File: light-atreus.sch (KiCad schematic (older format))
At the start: 1 part

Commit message: Completely redesign everything
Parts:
- removed U?: TUSB320, symbol TUSB320
- added J? (x2): USB_OTG, symbol USB_OTG
- added J? (x2): CONN_01X02, symbol CONN_01X02
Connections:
- net labels added: GND
- wire segments 0 -> 14
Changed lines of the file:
@@
 LIBS:valves
 LIBS:project
-EELAYER 25 0
+LIBS:light-atreus-cache
+EELAYER 26 0
 EELAYER END
 $Descr A4 11693 8268
@@
 $EndDescr
 $Comp
-L TUSB320 U?
-U 1 1 597ED03E
-P 5950 3850
-F 0 "U?" H 6350 4400 60  0000 C CNN
-F 1 "TUSB320" H 5450 4300 60  0000 C CNN
-F 2 "" H 5550 3900 60  0001 C CNN
-F 3 "" H 5550 3900 60  0001 C CNN
-	1    5950 3850
+L USB_OTG J?
+U 1 1 59C6CA5B
+P 3500 3850
+F 0 "J?" H 3555 4317 50  0000 C CNN
+F 1 "USB_OTG" H 3555 4226 50  0000 C CNN
+F 2 "" H 3650 3800 50  0001 C CNN
+F 3 "" H 3650 3800 50  0001 C CNN
+	1    3500 3850
 	1    0    0    -1
 $EndComp
+$Comp
+L USB_OTG J?
+U 1 1 59C6CAF0
+P 6000 3850
+F 0 "J?" H 6056 4317 50  0000 C CNN
+F 1 "USB_OTG" H 6056 4226 50  0000 C CNN
+F 2 "" H 6150 3800 50  0001 C CNN
+F 3 "" H 6150 3800 50  0001 C CNN
+	1    6000 3850
+	-1   0    0    -1
+$EndComp
+Wire Wire Line
+	3800 3650 5700 3650
+Wire Wire Line
+	3800 3850 5700 3850
+Wire Wire Line
+	3800 3950 5700 3950
+Wire Wire Line
+	3800 4050 5700 4050
+Wire Wire Line
+	3500 4250 3500 4350
+Wire Wire Line
+	3500 4350 6000 4350
+Wire Wire Line
+	6000 4350 6000 4250
+Wire Wire Line
+	3400 4250 3400 4450
+Wire Wire Line
+	3400 4450 6100 4450
+Wire Wire Line
+	6100 4450 6100 4250
+Wire Wire Line
+	4750 3350 4750 4550
+Connection ~ 4750 4450
+Connection ~ 4750 4350
+$Comp
+L GND #PWR?
+U 1 1 59C6CDCA
+P 4750 4550
+F 0 "#PWR?" H 4750 4300 50  0001 C CNN
+F 1 "GND" H 4755 4377 50  0000 C CNN
+F 2 "" H 4750 4550 50  0001 C CNN
+F 3 "" H 4750 4550 50  0001 C CNN
+	1    4750 4550
+	1    0    0    -1
+$EndComp
+$Comp
+L CONN_01X02 J?
+U 1 1 59C6CECB
+P 5050 3300
+F 0 "J?" H 5128 3341 50  0000 L CNN
+F 1 "CONN_01X02" H 5128 3250 50  0000 L CNN
+F 2 "" H 5050 3300 50  0001 C CNN
+F 3 "" H 5050 3300 50  0001 C CNN
+	1    5050 3300
+	1    0    0    -1
+$EndComp
+Wire Wire Line
+	4400 3250 4850 3250
+Wire Wire Line
+	4600 3250 4600 3650
+Connection ~ 4600 3650
+Wire Wire Line
+	4400 3350 4850 3350
+$Comp
+L CONN_01X02 J?
+U 1 1 59C6D03C
+P 4200 3300
+F 0 "J?" H 4278 3341 50  0000 L CNN
+F 1 "CONN_01X02" H 4278 3250 50  0000 L CNN
+F 2 "" H 4200 3300 50  0001 C CNN
+F 3 "" H 4200 3300 50  0001 C CNN
+	1    4200 3300
+	-1   0    0    -1
+$EndComp
+Connection ~ 4750 3350
+Connection ~ 4600 3250
 $EndSCHEMATC

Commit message: Use 4-pin connectors for doing fish-hook
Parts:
- removed J? (x2): CONN_01X02, symbol CONN_01X02
- added J? (x2): CONN_01X04, symbol CONN_01X04
- J? (x2): footprint (none) -> Connectors:USB_Micro-B
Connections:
- net labels removed: GND
- no-connect marks 0 -> 4
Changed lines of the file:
@@
 F 0 "J?" H 3555 4317 50  0000 C CNN
 F 1 "USB_OTG" H 3555 4226 50  0000 C CNN
-F 2 "" H 3650 3800 50  0001 C CNN
+F 2 "Connectors:USB_Micro-B" H 3650 3800 50  0001 C CNN
 F 3 "" H 3650 3800 50  0001 C CNN
 	1    3500 3850
@@
 F 0 "J?" H 6056 4317 50  0000 C CNN
 F 1 "USB_OTG" H 6056 4226 50  0000 C CNN
-F 2 "" H 6150 3800 50  0001 C CNN
+F 2 "Connectors:USB_Micro-B" H 6150 3800 50  0001 C CNN
 F 3 "" H 6150 3800 50  0001 C CNN
 	1    6000 3850
@@
 	3800 3950 5700 3950
 Wire Wire Line
-	3800 4050 5700 4050
-Wire Wire Line
 	3500 4250 3500 4350
 Wire Wire Line
@@
 	3400 4250 3400 4450
 Wire Wire Line
-	3400 4450 6100 4450
-Wire Wire Line
 	6100 4450 6100 4250
-Wire Wire Line
-	4750 3350 4750 4550
-Connection ~ 4750 4450
-Connection ~ 4750 4350
-$Comp
-L GND #PWR?
-U 1 1 59C6CDCA
-P 4750 4550
-F 0 "#PWR?" H 4750 4300 50  0001 C CNN
-F 1 "GND" H 4755 4377 50  0000 C CNN
-F 2 "" H 4750 4550 50  0001 C CNN
-F 3 "" H 4750 4550 50  0001 C CNN
-	1    4750 4550
-	1    0    0    -1
-$EndComp
-$Comp
-L CONN_01X02 J?
-U 1 1 59C6CECB
-P 5050 3300
-F 0 "J?" H 5128 3341 50  0000 L CNN
-F 1 "CONN_01X02" H 5128 3250 50  0000 L CNN
-F 2 "" H 5050 3300 50  0001 C CNN
-F 3 "" H 5050 3300 50  0001 C CNN
-	1    5050 3300
-	1    0    0    -1
-$EndComp
 Wire Wire Line
 	4400 3250 4850 3250
@@
 Wire Wire Line
 	4400 3350 4850 3350
+Connection ~ 4750 3350
+Connection ~ 4600 3250
 $Comp
-L CONN_01X02 J?
-U 1 1 59C6D03C
+L CONN_01X04 J?
+U 1 1 59C6D991
+P 5050 3300
+F 0 "J?" H 5128 3341 50  0000 L CNN
+F 1 "CONN_01X04" H 5128 3250 50  0000 L CNN
+F 2 "" H 5050 3300 50  0001 C CNN
+F 3 "" H 5050 3300 50  0001 C CNN
+	1    5050 3300
+	1    0    0    -1
+$EndComp
+$Comp
+L CONN_01X04 J?
+U 1 1 59C6D9ED
 P 4200 3300
 F 0 "J?" H 4278 3341 50  0000 L CNN
-F 1 "CONN_01X02" H 4278 3250 50  0000 L CNN
+F 1 "CONN_01X04" H 4278 3250 50  0000 L CNN
 F 2 "" H 4200 3300 50  0001 C CNN
 F 3 "" H 4200 3300 50  0001 C CNN
@@
 	-1   0    0    -1
 $EndComp
-Connection ~ 4750 3350
-Connection ~ 4600 3250
+NoConn ~ 4850 3450
+NoConn ~ 4850 3150
+NoConn ~ 4400 3150
+NoConn ~ 4400 3450
+Wire Wire Line
+	3400 4450 6100 4450
+Wire Wire Line
+	4750 3350 4750 4350
+Connection ~ 4750 4350
+Wire Wire Line
+	3800 4050 5700 4050
 $EndSCHEMATC

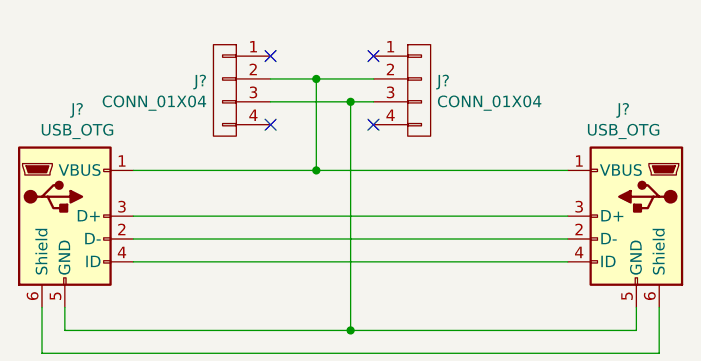
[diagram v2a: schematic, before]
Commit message: Use 2x2 instead of 1x4 headers
That way the arrangement will put the holder hole nearer to the outer
edge of the board.
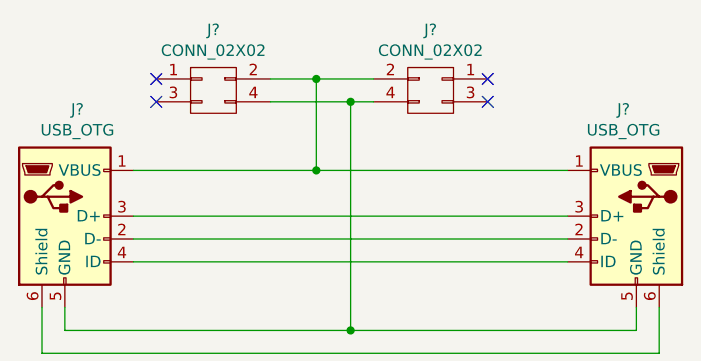
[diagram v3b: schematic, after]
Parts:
- removed J? (x2): CONN_01X04, symbol CONN_01X04
- added J? (x2): CONN_02X02, symbol CONN_02X02
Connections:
- net at J?.1 (VBUS), J?.1 (VBUS): now also J?.2 (P2), J?.2 (P2)
- net at J?.5 (GND), J?.5 (GND): now also J?.4 (P4), J?.4 (P4)
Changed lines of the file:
@@
 Connection ~ 4750 3350
 Connection ~ 4600 3250
-$Comp
-L CONN_01X04 J?
-U 1 1 59C6D991
-P 5050 3300
-F 0 "J?" H 5128 3341 50  0000 L CNN
-F 1 "CONN_01X04" H 5128 3250 50  0000 L CNN
-F 2 "" H 5050 3300 50  0001 C CNN
-F 3 "" H 5050 3300 50  0001 C CNN
-	1    5050 3300
-	1    0    0    -1
-$EndComp
-$Comp
-L CONN_01X04 J?
-U 1 1 59C6D9ED
-P 4200 3300
-F 0 "J?" H 4278 3341 50  0000 L CNN
-F 1 "CONN_01X04" H 4278 3250 50  0000 L CNN
-F 2 "" H 4200 3300 50  0001 C CNN
-F 3 "" H 4200 3300 50  0001 C CNN
-	1    4200 3300
-	-1   0    0    -1
-$EndComp
-NoConn ~ 4850 3450
-NoConn ~ 4850 3150
-NoConn ~ 4400 3150
-NoConn ~ 4400 3450
 Wire Wire Line
 	3400 4450 6100 4450
@@
 Wire Wire Line
 	3800 4050 5700 4050
+$Comp
+L CONN_02X02 J?
+U 1 1 59CAC2E2
+P 4150 3300
+F 0 "J?" H 4150 3565 50  0000 C CNN
+F 1 "CONN_02X02" H 4150 3474 50  0000 C CNN
+F 2 "" H 4150 2100 50  0001 C CNN
+F 3 "" H 4150 2100 50  0001 C CNN
+	1    4150 3300
+	1    0    0    -1
+$EndComp
+$Comp
+L CONN_02X02 J?
+U 1 1 59CAC352
+P 5100 3300
+F 0 "J?" H 5100 3565 50  0000 C CNN
+F 1 "CONN_02X02" H 5100 3474 50  0000 C CNN
+F 2 "" H 5100 2100 50  0001 C CNN
+F 3 "" H 5100 2100 50  0001 C CNN
+	1    5100 3300
+	-1   0    0    -1
+$EndComp
+NoConn ~ 5350 3250
+NoConn ~ 5350 3350
+NoConn ~ 3900 3350
+NoConn ~ 3900 3250
 $EndSCHEMATC

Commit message: Annotate and generate netlist
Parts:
- gave numbers to parts that had none: 4
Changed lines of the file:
@@
 $EndDescr
 $Comp
-L USB_OTG J?
+L USB_OTG J1
 U 1 1 59C6CA5B
 P 3500 3850
-F 0 "J?" H 3555 4317 50  0000 C CNN
+F 0 "J1" H 3555 4317 50  0000 C CNN
 F 1 "USB_OTG" H 3555 4226 50  0000 C CNN
 F 2 "Connectors:USB_Micro-B" H 3650 3800 50  0001 C CNN
@@
 $EndComp
 $Comp
-L USB_OTG J?
+L USB_OTG J4
 U 1 1 59C6CAF0
 P 6000 3850
-F 0 "J?" H 6056 4317 50  0000 C CNN
+F 0 "J4" H 6056 4317 50  0000 C CNN
 F 1 "USB_OTG" H 6056 4226 50  0000 C CNN
 F 2 "Connectors:USB_Micro-B" H 6150 3800 50  0001 C CNN
@@
 	3800 4050 5700 4050
 $Comp
-L CONN_02X02 J?
+L CONN_02X02 J2
 U 1 1 59CAC2E2
 P 4150 3300
-F 0 "J?" H 4150 3565 50  0000 C CNN
+F 0 "J2" H 4150 3565 50  0000 C CNN
 F 1 "CONN_02X02" H 4150 3474 50  0000 C CNN
 F 2 "" H 4150 2100 50  0001 C CNN
@@
 $EndComp
 $Comp
-L CONN_02X02 J?
+L CONN_02X02 J3
 U 1 1 59CAC352
 P 5100 3300
-F 0 "J?" H 5100 3565 50  0000 C CNN
+F 0 "J3" H 5100 3565 50  0000 C CNN
 F 1 "CONN_02X02" H 5100 3474 50  0000 C CNN
 F 2 "" H 5100 2100 50  0001 C CNN

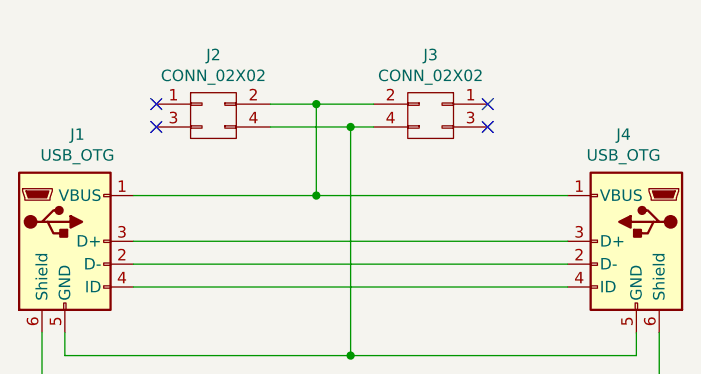
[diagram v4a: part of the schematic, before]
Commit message: Use banana jack connector pads
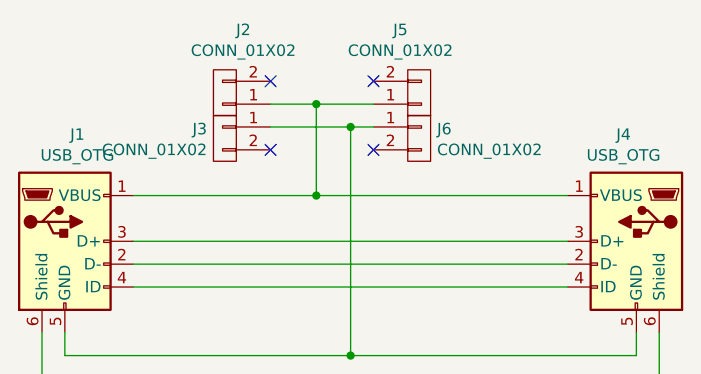
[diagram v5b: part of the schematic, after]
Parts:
- removed J2, J3: CONN_02X02, symbol CONN_02X02
- added J2, J3, J5, J6: CONN_01X02, Connectors:Banana_Jack_2Pin, symbol CONN_01X02
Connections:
- net at J1.1 (VBUS), J4.1 (VBUS): now also J2.1 (P1), J5.1 (P1)
- net at J1.5 (GND), J4.5 (GND): now also J3.1 (P1), J6.1 (P1)
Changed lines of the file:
@@
 	3800 4050 5700 4050
 $Comp
-L CONN_02X02 J2
-U 1 1 59CAC2E2
-P 4150 3300
-F 0 "J2" H 4150 3565 50  0000 C CNN
-F 1 "CONN_02X02" H 4150 3474 50  0000 C CNN
-F 2 "" H 4150 2100 50  0001 C CNN
-F 3 "" H 4150 2100 50  0001 C CNN
-	1    4150 3300
+L CONN_01X02 J2
+U 1 1 59CAC5DC
+P 4200 3200
+F 0 "J2" H 4119 2925 50  0000 C CNN
+F 1 "CONN_01X02" H 4119 3016 50  0000 C CNN
+F 2 "Connectors:Banana_Jack_2Pin" H 4200 3200 50  0001 C CNN
+F 3 "" H 4200 3200 50  0001 C CNN
+	1    4200 3200
+	-1   0    0    1
+$EndComp
+$Comp
+L CONN_01X02 J3
+U 1 1 59CAC664
+P 4200 3400
+F 0 "J3" H 4278 3441 50  0000 L CNN
+F 1 "CONN_01X02" H 4278 3350 50  0000 L CNN
+F 2 "Connectors:Banana_Jack_2Pin" H 4200 3400 50  0001 C CNN
+F 3 "" H 4200 3400 50  0001 C CNN
+	1    4200 3400
+	-1   0    0    -1
+$EndComp
+$Comp
+L CONN_01X02 J5
+U 1 1 59CAC690
+P 5050 3200
+F 0 "J5" H 4968 2925 50  0000 C CNN
+F 1 "CONN_01X02" H 4968 3016 50  0000 C CNN
+F 2 "Connectors:Banana_Jack_2Pin" H 5050 3200 50  0001 C CNN
+F 3 "" H 5050 3200 50  0001 C CNN
+	1    5050 3200
+	1    0    0    1
+$EndComp
+$Comp
+L CONN_01X02 J6
+U 1 1 59CAC6F5
+P 5050 3400
+F 0 "J6" H 5128 3441 50  0000 L CNN
+F 1 "CONN_01X02" H 5128 3350 50  0000 L CNN
+F 2 "Connectors:Banana_Jack_2Pin" H 5050 3400 50  0001 C CNN
+F 3 "" H 5050 3400 50  0001 C CNN
+	1    5050 3400
 	1    0    0    -1
 $EndComp
-$Comp
-L CONN_02X02 J3
-U 1 1 59CAC352
-P 5100 3300
-F 0 "J3" H 5100 3565 50  0000 C CNN
-F 1 "CONN_02X02" H 5100 3474 50  0000 C CNN
-F 2 "" H 5100 2100 50  0001 C CNN
-F 3 "" H 5100 2100 50  0001 C CNN
-	1    5100 3300
-	-1   0    0    -1
-$EndComp
-NoConn ~ 5350 3250
-NoConn ~ 5350 3350
-NoConn ~ 3900 3350
-NoConn ~ 3900 3250
+NoConn ~ 4850 3450
+NoConn ~ 4850 3150
+NoConn ~ 4400 3150
+NoConn ~ 4400 3450
 $EndSCHEMATC

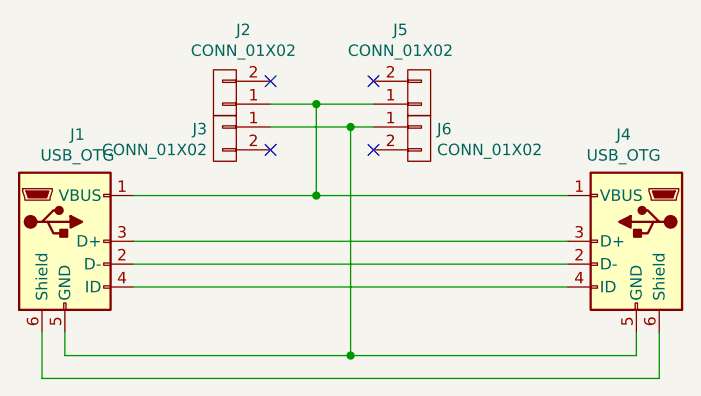
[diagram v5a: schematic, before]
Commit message: Name nets on broken out pins
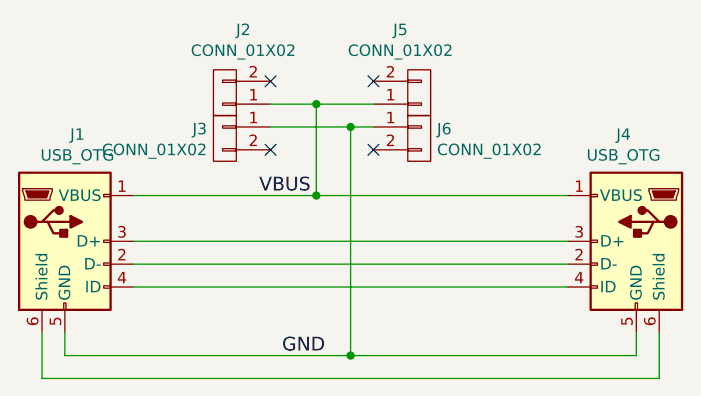
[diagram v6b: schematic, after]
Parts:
- J2, J3, J5, J6: footprint Connectors:Banana_Jack_2Pin -> custom_footprints:SolderWirePad_1x2-8mm
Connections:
- net VBUS: now reaches J1.1 (VBUS), J2.1 (P1), J4.1 (VBUS), J5.1 (P1)
- net GND: now reaches J1.5 (GND), J3.1 (P1), J4.5 (GND), J6.1 (P1)
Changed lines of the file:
@@
 F 0 "J2" H 4119 2925 50  0000 C CNN
 F 1 "CONN_01X02" H 4119 3016 50  0000 C CNN
-F 2 "Connectors:Banana_Jack_2Pin" H 4200 3200 50  0001 C CNN
+F 2 "custom_footprints:SolderWirePad_1x2-8mm" H 4200 3200 50  0001 C CNN
 F 3 "" H 4200 3200 50  0001 C CNN
 	1    4200 3200
@@
 F 0 "J3" H 4278 3441 50  0000 L CNN
 F 1 "CONN_01X02" H 4278 3350 50  0000 L CNN
-F 2 "Connectors:Banana_Jack_2Pin" H 4200 3400 50  0001 C CNN
+F 2 "custom_footprints:SolderWirePad_1x2-8mm" H 4200 3400 50  0001 C CNN
 F 3 "" H 4200 3400 50  0001 C CNN
 	1    4200 3400
@@
 F 0 "J5" H 4968 2925 50  0000 C CNN
 F 1 "CONN_01X02" H 4968 3016 50  0000 C CNN
-F 2 "Connectors:Banana_Jack_2Pin" H 5050 3200 50  0001 C CNN
+F 2 "custom_footprints:SolderWirePad_1x2-8mm" H 5050 3200 50  0001 C CNN
 F 3 "" H 5050 3200 50  0001 C CNN
 	1    5050 3200
@@
 F 0 "J6" H 5128 3441 50  0000 L CNN
 F 1 "CONN_01X02" H 5128 3350 50  0000 L CNN
-F 2 "Connectors:Banana_Jack_2Pin" H 5050 3400 50  0001 C CNN
+F 2 "custom_footprints:SolderWirePad_1x2-8mm" H 5050 3400 50  0001 C CNN
 F 3 "" H 5050 3400 50  0001 C CNN
 	1    5050 3400
@@
 NoConn ~ 4400 3150
 NoConn ~ 4400 3450
+Text Label 4450 4350 0    60   ~ 0
+GND
+Text Label 4350 3650 0    60   ~ 0
+VBUS
 $EndSCHEMATC

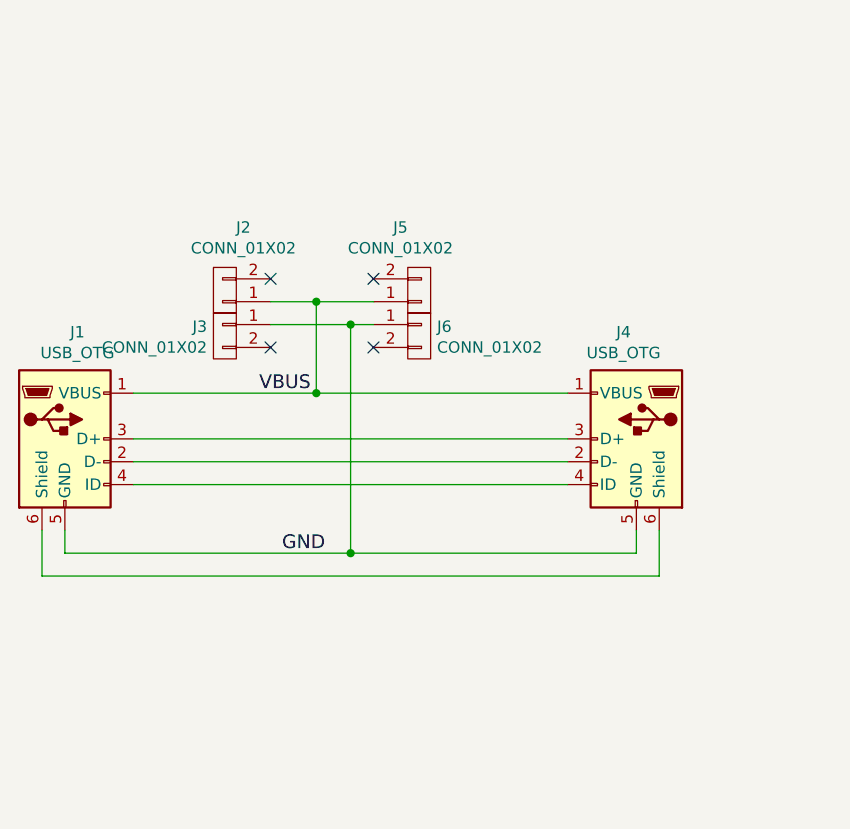
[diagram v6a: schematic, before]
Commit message: Update schematic for allowing hand-wiring USB plug
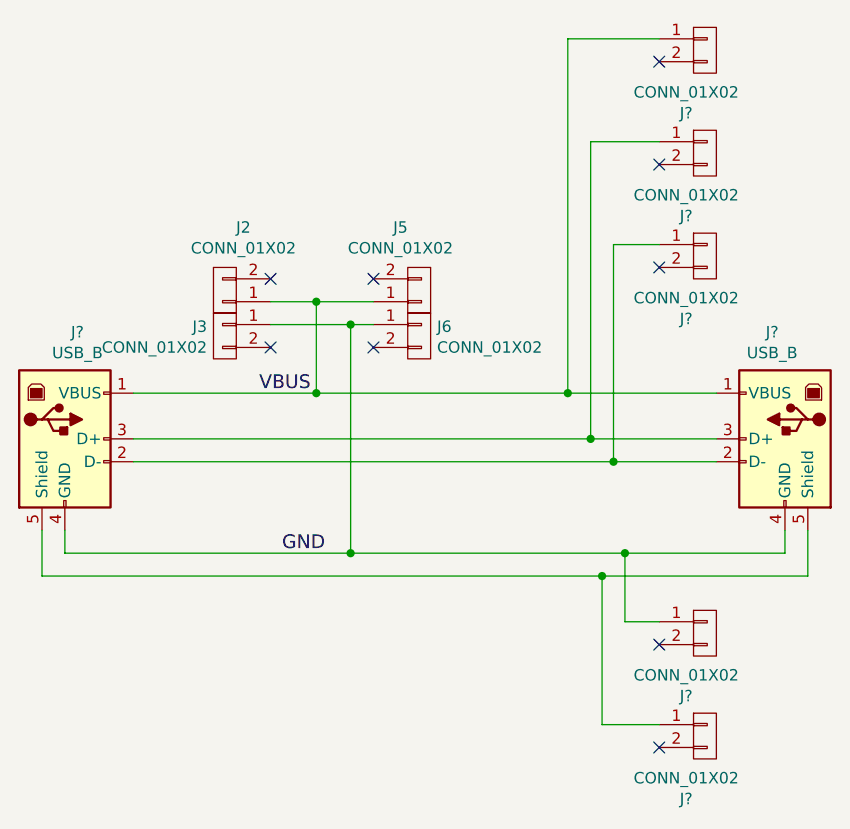
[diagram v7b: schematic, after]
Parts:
- removed J1, J4: USB_OTG, Connectors:USB_Micro-B, symbol USB_OTG
- added J?: USB_B, custom_footprints:USB_Micro-B-custom, symbol USB_B
- added J?: USB_B, symbol USB_B
- added J? (x5): CONN_01X02, custom_footprints:SolderWirePad_1x2-8mm, symbol CONN_01X02
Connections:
- net GND: now also J?.1 (P1), J?.4 (GND), J?.4 (GND)
- net VBUS: now also J?.1 (P1), J?.1 (VBUS), J?.1 (VBUS)
- new net: J?.1 (P1), J?.2 (D-), J?.2 (D-)
- new net: J?.1 (P1), J?.3 (D+), J?.3 (D+)
- new net: J?.1 (P1), J?.5 (Shield), J?.5 (Shield)
- no-connect marks 4 -> 9
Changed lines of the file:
@@
 Comment4 ""
 $EndDescr
-$Comp
-L USB_OTG J1
-U 1 1 59C6CA5B
-P 3500 3850
-F 0 "J1" H 3555 4317 50  0000 C CNN
-F 1 "USB_OTG" H 3555 4226 50  0000 C CNN
-F 2 "Connectors:USB_Micro-B" H 3650 3800 50  0001 C CNN
-F 3 "" H 3650 3800 50  0001 C CNN
-	1    3500 3850
-	1    0    0    -1
-$EndComp
-$Comp
-L USB_OTG J4
-U 1 1 59C6CAF0
-P 6000 3850
-F 0 "J4" H 6056 4317 50  0000 C CNN
-F 1 "USB_OTG" H 6056 4226 50  0000 C CNN
-F 2 "Connectors:USB_Micro-B" H 6150 3800 50  0001 C CNN
-F 3 "" H 6150 3800 50  0001 C CNN
-	1    6000 3850
-	-1   0    0    -1
-$EndComp
 Wire Wire Line
-	3800 3650 5700 3650
+	3800 3650 6350 3650
 Wire Wire Line
-	3800 3850 5700 3850
+	3800 3850 6350 3850
 Wire Wire Line
-	3800 3950 5700 3950
+	3800 3950 6350 3950
 Wire Wire Line
 	3500 4250 3500 4350
 Wire Wire Line
-	3500 4350 6000 4350
-Wire Wire Line
-	6000 4350 6000 4250
+	3500 4350 6650 4350
 Wire Wire Line
 	3400 4250 3400 4450
-Wire Wire Line
-	6100 4450 6100 4250
 Wire Wire Line
 	4400 3250 4850 3250
@@
 Connection ~ 4600 3250
 Wire Wire Line
-	3400 4450 6100 4450
-Wire Wire Line
 	4750 3350 4750 4350
 Connection ~ 4750 4350
-Wire Wire Line
-	3800 4050 5700 4050
 $Comp
 L CONN_01X02 J2
@@
 Text Label 4350 3650 0    60   ~ 0
 VBUS
+$Comp
+L USB_B J?
+U 1 1 59CD5E46
+P 3500 3850
+F 0 "J?" H 3555 4317 50  0000 C CNN
+F 1 "USB_B" H 3555 4226 50  0000 C CNN
+F 2 "custom_footprints:USB_Micro-B-custom" H 3650 3800 50  0001 C CNN
+F 3 "" H 3650 3800 50  0001 C CNN
+	1    3500 3850
+	1    0    0    -1
+$EndComp
+$Comp
+L USB_B J?
+U 1 1 59CD612E
+P 6650 3850
+F 0 "J?" H 6706 4317 50  0000 C CNN
+F 1 "USB_B" H 6706 4226 50  0000 C CNN
+F 2 "" H 6800 3800 50  0001 C CNN
+F 3 "" H 6800 3800 50  0001 C CNN
+	1    6650 3850
+	-1   0    0    -1
+$EndComp
+$Comp
+L CONN_01X02 J?
+U 1 1 59CD62AF
+P 6300 3050
+F 0 "J?" H 6218 2775 50  0000 C CNN
+F 1 "CONN_01X02" H 6218 2866 50  0000 C CNN
+F 2 "custom_footprints:SolderWirePad_1x2-8mm" H 6300 3050 50  0001 C CNN
+F 3 "" H 6300 3050 50  0001 C CNN
+	1    6300 3050
+	1    0    0    -1
+$EndComp
+Wire Wire Line
+	3400 4450 6750 4450
+Wire Wire Line
+	6650 4350 6650 4250
+Wire Wire Line
+	6750 4450 6750 4250
+$Comp
+L CONN_01X02 J?
+U 1 1 59CD64BA
+P 6300 2600
+F 0 "J?" H 6218 2325 50  0000 C CNN
+F 1 "CONN_01X02" H 6218 2416 50  0000 C CNN
+F 2 "custom_footprints:SolderWirePad_1x2-8mm" H 6300 2600 50  0001 C CNN
+F 3 "" H 6300 2600 50  0001 C CNN
+	1    6300 2600
+	1    0    0    -1
+$EndComp
+$Comp
+L CONN_01X02 J?
+U 1 1 59CD6590
+P 6300 4700
+F 0 "J?" H 6218 4425 50  0000 C CNN
+F 1 "CONN_01X02" H 6218 4516 50  0000 C CNN
+F 2 "custom_footprints:SolderWirePad_1x2-8mm" H 6300 4700 50  0001 C CNN
+F 3 "" H 6300 4700 50  0001 C CNN
+	1    6300 4700
+	1    0    0    -1
+$EndComp
+$Comp
+L CONN_01X02 J?
+U 1 1 59CD667D
+P 6300 5150
+F 0 "J?" H 6218 4875 50  0000 C CNN
+F 1 "CONN_01X02" H 6218 4966 50  0000 C CNN
+F 2 "custom_footprints:SolderWirePad_1x2-8mm" H 6300 5150 50  0001 C CNN
+F 3 "" H 6300 5150 50  0001 C CNN
+	1    6300 5150
+	1    0    0    -1
+$EndComp
+$Comp
+L CONN_01X02 J?
+U 1 1 59CD691B
+P 6300 2150
+F 0 "J?" H 6218 1875 50  0000 C CNN
+F 1 "CONN_01X02" H 6218 1966 50  0000 C CNN
+F 2 "custom_footprints:SolderWirePad_1x2-8mm" H 6300 2150 50  0001 C CNN
+F 3 "" H 6300 2150 50  0001 C CNN
+	1    6300 2150
+	1    0    0    -1
+$EndComp
+Wire Wire Line
+	6100 2100 5700 2100
+Wire Wire Line
+	5700 2100 5700 3650
+Connection ~ 5700 3650
+Wire Wire Line
+	6100 2550 5800 2550
+Wire Wire Line
+	5800 2550 5800 3850
+Connection ~ 5800 3850
+Wire Wire Line
+	6100 3000 5900 3000
+Wire Wire Line
+	5900 3000 5900 3950
+Connection ~ 5900 3950
+NoConn ~ 6100 3100
+NoConn ~ 6100 2650
+NoConn ~ 6100 2200
+NoConn ~ 6100 4750
+NoConn ~ 6100 5200
+Wire Wire Line
+	6100 4650 5950 4650
+Wire Wire Line
+	5950 4650 5950 4350
+Connection ~ 5950 4350
+Wire Wire Line
+	6100 5100 5850 5100
+Wire Wire Line
+	5850 5100 5850 4450
+Connection ~ 5850 4450
 $EndSCHEMATC
